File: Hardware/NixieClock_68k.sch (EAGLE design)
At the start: 70 parts, among them IC1 68008, IC10 7805, IC11 MIC803, IC2 AS6C1008, IC3 39SF020, IC4 DS1244Y, IC5 FT245R, IC6 NE555, IC7 ATF1504AS, IC8 74HC374N, IC9 74HC373N, X1 4MHz

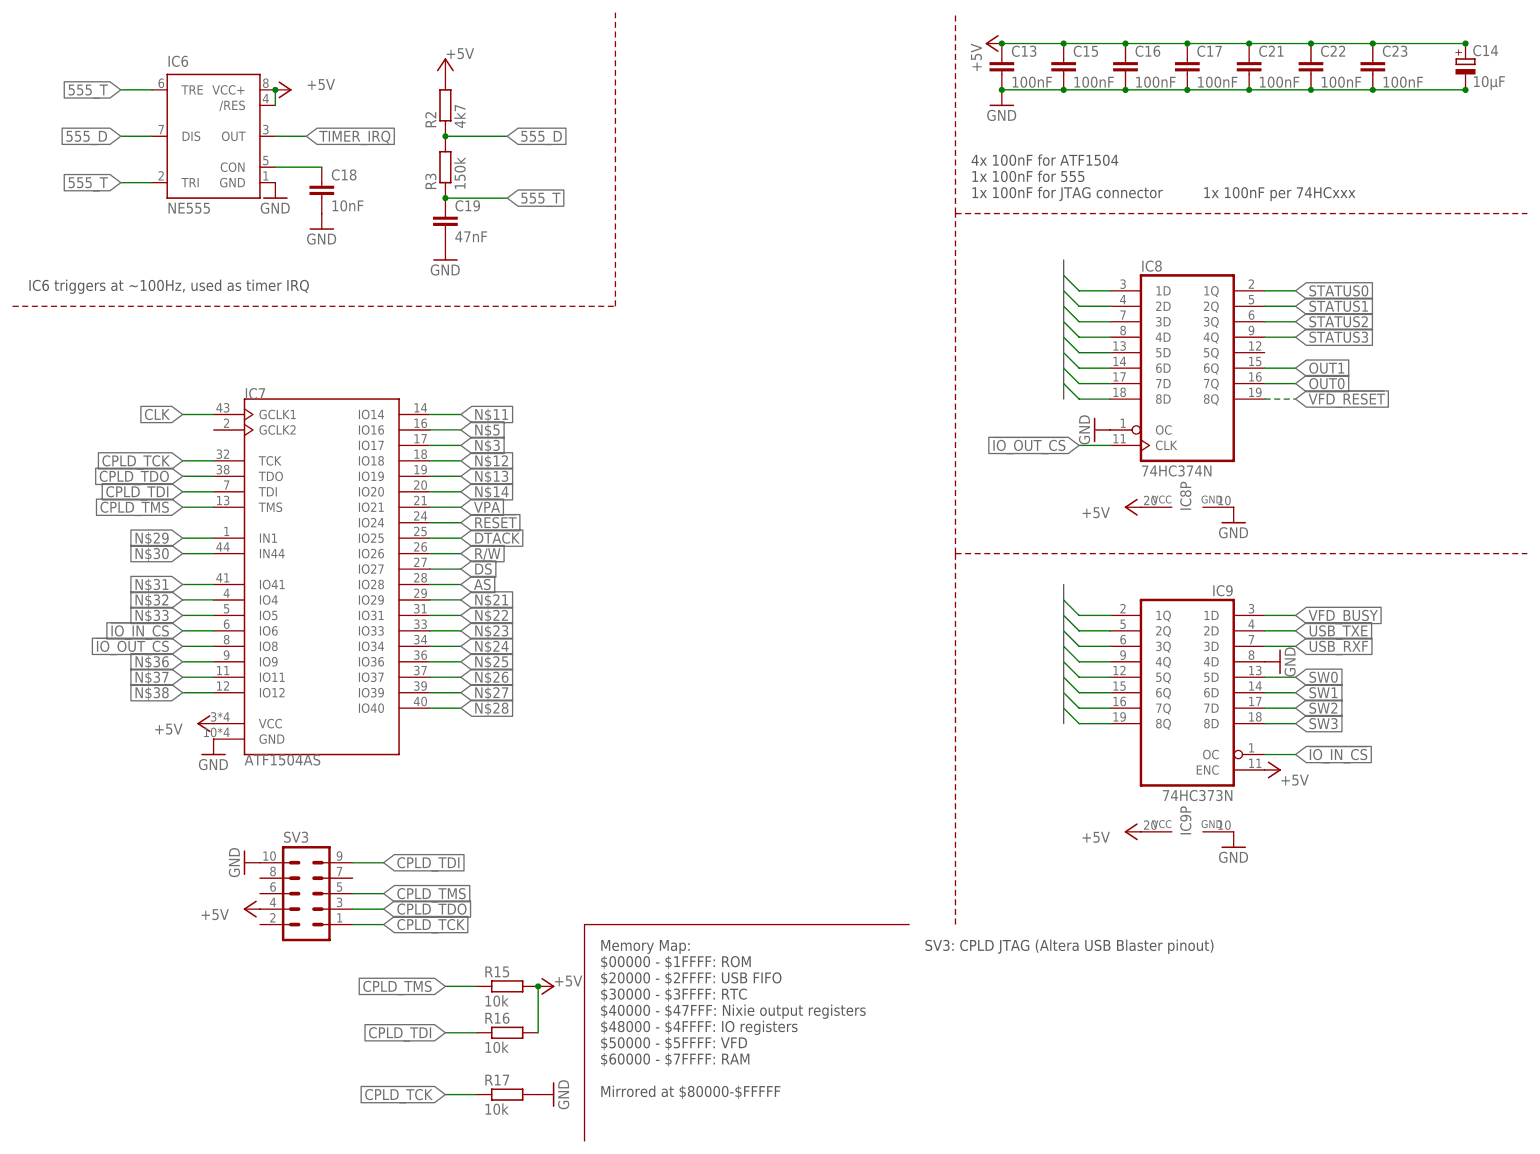
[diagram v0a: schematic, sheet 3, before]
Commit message: replaced cpld with ttl logic
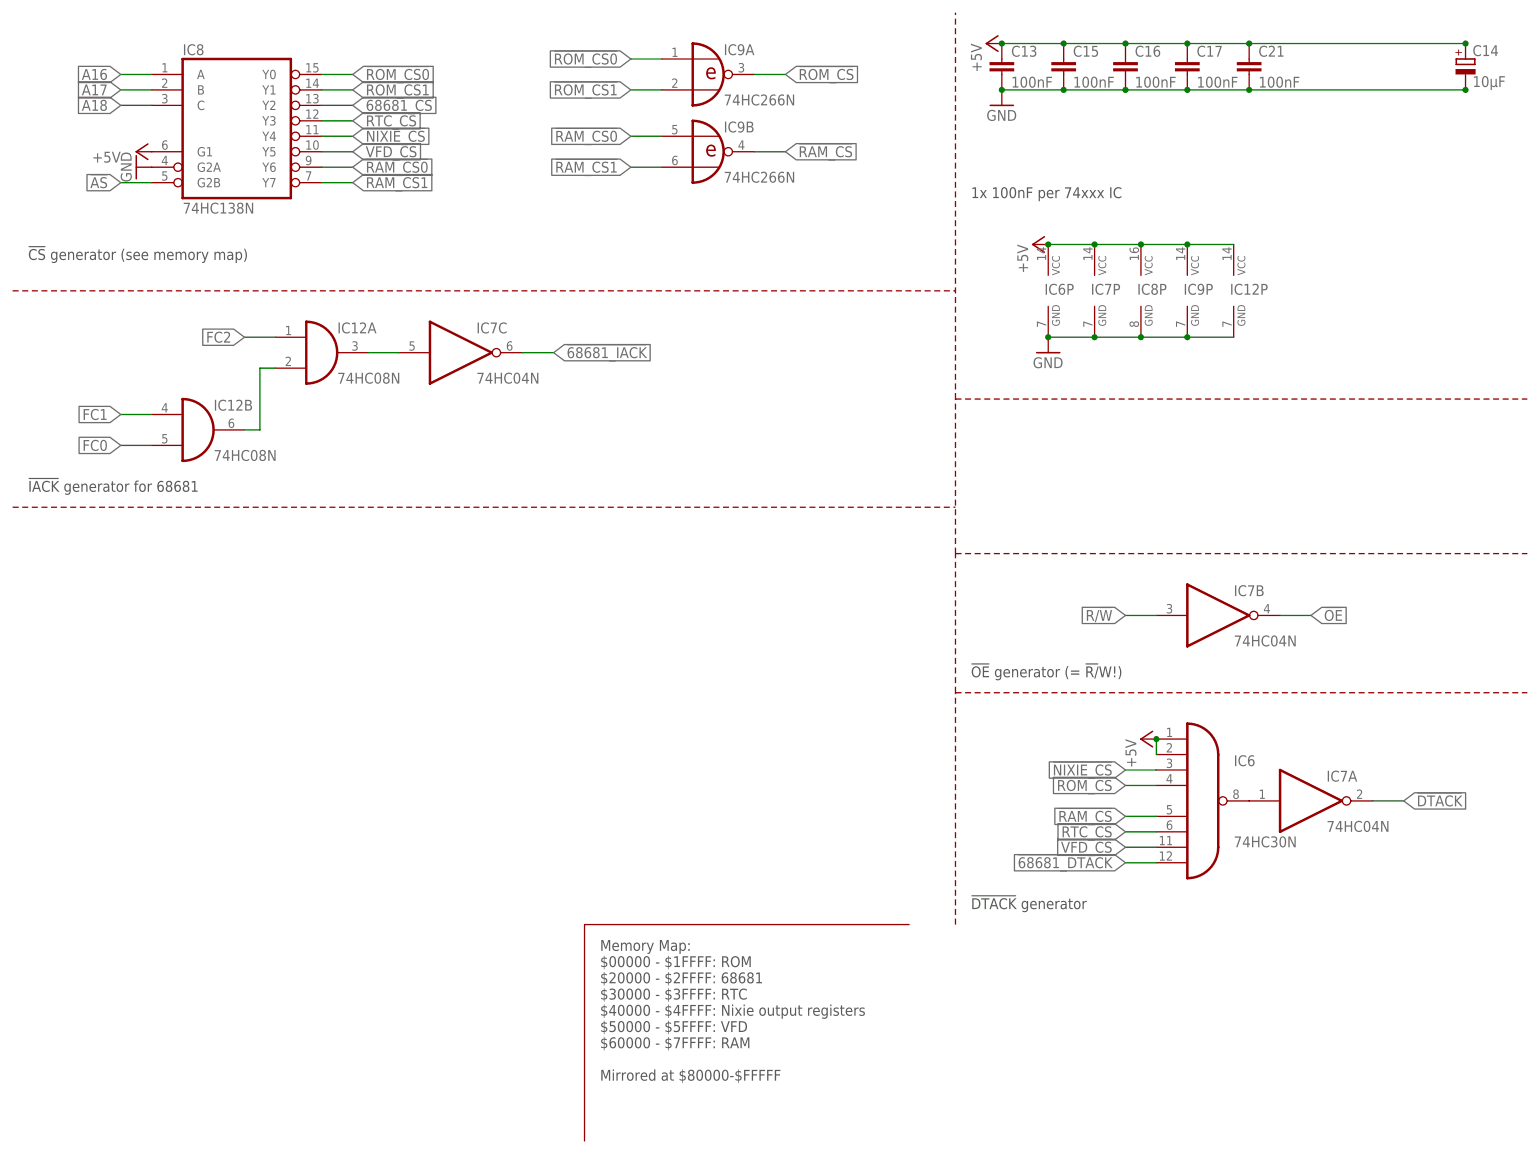
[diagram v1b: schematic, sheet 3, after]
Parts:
- removed C19: 47nF, rcl:C-EUC0805
- removed C22, C23: 100nF, rcl:C-EUC0805
- removed R14, R15, R16, R17, R18, R21, R22, R23, R5, R6: 10k, rcl:R-EU_R2012
- removed R20: 4k7, rcl:R-EU_R2012
- removed R3: 150k, rcl:R-EU_R2012
- removed SV3: (no value), con-lstb:MA05-2
- added IC12: 74HC08N, 74xx-eu:74HC08N
- added Q2: 3.6864MHz, crystal:CRYSTALHC49S
- C12: value 100nF -> 27pF; MOUSER 710-885012207072 -> 77-VJ0805A270GXQCBC
- C18: value 10nF -> 27pF; MOUSER 710-885342207010 -> 77-VJ0805A270GXQCBC
- IC5: value FT245R -> 68681; device Parts:FT245RSSOP-28 -> Parts:MC68681PLCC44-SOCKET
- IC6: value NE555 -> 74HC30N; device st-microelectronics:NE555 -> 74xx-eu:74HC30N; MOUSER 595-NE555P -> 595-CD74HC30E
- IC7: value ATF1504AS -> 74HC04N; device Parts:ATF1504ASPLCC44-SOCKET -> 74xx-eu:74HC04N; MOUSER (none) -> 595-SN74HC04AN
- IC8: value 74HC374N -> 74HC138N; device 74xx-eu:74HC374N -> 74xx-eu:74HC138N; MOUSER 595-SN74HC574N -> 595-SN74HC138N
- IC9: value 74HC373N -> 74HC266N; device 74xx-eu:74HC373N -> 74xx-eu:74HC266N; MOUSER 595-SN74HC373N -> 595-SN74HC266N
- R1: value 10k -> 100R; MOUSER 652-CR0805FX-1002ELF -> 652-CR0805FX-1000ELF
- R2: value 4k7 -> 100R; MOUSER 652-CR0805-JW-472ELF -> 652-CR0805FX-1000ELF
- SV5: value PN61729-S -> (none); device con-berg:PN61729-S -> con-lstb:MA04-2; MOUSER 649-61729-0010BLF -> (none)
- renumbered X1 to Q1
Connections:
- removed net !BERR: IC1.BERR, R14.1
- removed net !BR: IC1.BR, R18.1
- removed net !IO_IN_CS: IC7.IO6, IC9A.OC
- removed net !IO_OUT_CS: IC7.IO8, IC8A.CLK
- removed net !USB_PWREN: IC5.!PWREN, R1.1
- removed net !USB_RD: IC5.!RD
- removed net !USB_RESET: IC5.!RESET, R20.1, R21.2
- removed net !USB_RXF: IC5.!RXF, IC9A.3D, R6.1
- removed net !USB_TXE: IC5.!TXE, IC9A.2D, R5.1
- removed net !VFD_WR: SV2.5
- removed net !VPA: IC1.VPA, IC7.IO21, R22.1
- removed net 555_D: IC6.DIS, R2.1, R3.2
- removed net 555_T: C19.1, IC6.TRE, IC6.TRI, R3.1
- removed net CPLD_TCK: IC7.TCK, R17.1, SV3.1
- removed net CPLD_TDI: IC7.TDI, R16.1, SV3.9
- removed net CPLD_TDO: IC7.TDO, SV3.3
- removed net CPLD_TMS: IC7.TMS, R15.1, SV3.5
- removed net N$10: R20.2, SV5.1
- removed net N$12: IC7.IO18
- removed net N$13: IC7.IO19
- removed net N$14: IC7.IO20
- removed net N$21: IC7.IO29
- removed net N$22: IC7.IO31
- removed net N$23: IC7.IO33
- removed net N$24: IC7.IO34
- removed net N$25: IC7.IO36
- removed net N$26: IC7.IO37
- removed net N$27: IC7.IO39
- removed net N$28: IC7.IO40
- removed net N$29: IC7.IN1
- removed net N$30: IC7.IN44
- removed net N$31: IC7.IO41
- removed net N$32: IC7.IO4
- removed net N$33: IC7.IO5
- removed net N$36: IC7.IO9
- removed net N$37: IC7.IO11
- removed net N$38: IC7.IO12
- removed net TIMER_IRQ: IC6.OUT
- removed net USB+: IC5.USBD+, SV5.3
- removed net USB-: IC5.USBD-, SV5.2
- removed net USB_WR: IC5.WR
- new net !68681_CS: IC5.!CS, IC8A.Y2
- new net !68681_DTACK: IC5.!DTACK, IC6A.I7
- new net !68681_IACK: IC5.!IACK, IC7C.O
- new net !RAM_CS0: IC8A.Y6, IC9B.I0
- new net !RAM_CS1: IC8A.Y7, IC9B.I1
- new net !ROM_CS0: IC8A.Y0, IC9A.I0
- new net !ROM_CS1: IC8A.Y1, IC9A.I1
- new net !VFD_CS: IC6A.I6, IC8A.Y5, SV2.5
- new net 68681_X1: IC5.X1/CLK, R2.1
- new net 68681_X2: IC5.X2, R1.2
- new net UART0_RX: IC5.RXDA, SV5.2
- new net UART0_TX: IC5.TXDA, SV5.1
- new net UART1_RX: IC5.RXDB, SV5.4
- new net UART1_TX: IC5.TXDB, SV5.3
- net !AS: now also IC8A.G2B; no longer IC7.IO28
- net !DS: no longer IC7.IO27
- net !DTACK: now also IC7A.O; no longer IC7.IO25, R23.1
- net !IPL1: now also IC5.!INTR
- net !NIXIE_CS: now also IC6A.I2, IC8A.Y4
- net !OE: now also IC7B.O
- net !RAM_CS: now also IC6A.I4, IC9B.O
- net !RESET: now also IC5.!RESET; no longer IC7.IO24
- net !ROM_CS: now also IC6A.I3, IC9A.O
- net !RTC_CS: now also IC6A.I5, IC8A.Y3
- net !VFD_RESET: now also IC5.OP4; no longer IC8A.8Q
- net +5V: now also IC1.BERR, IC1.BR, IC1.VPA, IC12P.VCC, IC6A.I0, IC6A.I1, IC6P.VCC, IC7P.VCC, IC8A.G1, SV5.6, SV5.8; no longer C22.1, C23.1, IC5.VCCIO, IC6./RES, IC6.VCC+, IC7.VCC, IC9A.ENC, R1.2, R14.2, R15.2, R16.2, R18.2, R2.2, R22.2, R23.2, R6.2, SV3.4
- net A0: now also IC5.A1
- net A1: now also IC5.A2
- net A16: now also IC8A.A
- net A17: now also IC8A.B
- net A18: now also IC8A.C
- net A2: now also IC5.A3
- net A3: now also IC5.A4
- net CLK: no longer IC7.GCLK1
- net D0: no longer IC8A.1D, IC9A.1Q
- net D1: no longer IC8A.2D, IC9A.2Q
- net D2: no longer IC8A.3D, IC9A.3Q
- net D3: no longer IC8A.4D, IC9A.4Q
- net D4: no longer IC8A.5D, IC9A.5Q
- net D5: no longer IC8A.6D, IC9A.6Q
- net D6: no longer IC8A.7D, IC9A.7Q
- net D7: no longer IC8A.8D, IC9A.8Q
- net FC0: now also IC12B.I1
- net FC1: now also IC12B.I0
- net FC2: now also IC12A.I0
- net GND: now also C12.2, IC12P.GND, IC6P.GND, IC7P.GND, IC8A.G2A, SV5.5, SV5.7; no longer C12.1, C19.2, C22.2, C23.2, IC5.AGND, IC5.TEST, IC6.GND, IC7.GND, IC8A.OC, IC9A.4D, R17.2, R21.1, R5.2, SV3.10, SV5.4, SV5.S1, SV5.S2
- net N$1: now also C12.1, Q2.2, R1.1; no longer C12.2, IC5.3V3OUT
- net N$11: now also IC12A.I1, IC12B.O; no longer IC7.IO14
- net N$2: now also Q2.1, R2.2; no longer IC6.CON
- net N$3: now also IC6A.O, IC7A.I; no longer IC7.IO17
- net N$5: now also IC12A.O, IC7C.I; no longer IC7.IO16
- net OUT0: no longer IC8A.7Q
- net OUT1: no longer IC8A.6Q
- net R/!W!: now also IC5.R/!W, IC7B.I; no longer IC7.IO26
- net STATUS0: now also IC5.OP0; no longer IC8A.1Q
- net STATUS1: now also IC5.OP1, R7.1; no longer IC8A.2Q
- net STATUS2: now also IC5.OP2; no longer IC8A.3Q, R7.1
- net STATUS3: now also IC5.OP3; no longer IC8A.4Q
- net SW0: now also IC5.IP0; no longer IC9A.5D
- net SW1: now also IC5.IP1; no longer IC9A.6D
- net SW2: now also IC5.IP2; no longer IC9A.7D
- net SW3: now also IC5.IP4; no longer IC9A.8D
- net VFD_BUSY: now also IC5.IP3; no longer IC9A.1D
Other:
- note added: "!CS! generator (see memory map)"
- note added: "!DTACK! generator"
- note added: "!IACK! generator for 68681"
- note added: "!OE! generator (= !R/!W!)"
- note added: "1x 100nF per 74xxx IC"
- note added: "1x 10µF for VFD/Nixie connector 1x 10µF for 68681/DS1244Y 1x 100nF for each IC and connector"
- note added: "Memory Map: $00000 - $1FFFF: ROM $20000 - $2FFFF: 68681 $30000 - $3FFFF: RTC $40000 - $4FFFF: Nixie output registers $50000 - $5FFFF: VFD $60000 - $7FFFF: RAM Mirrored at $80000-$FFFFF"
- note added: "SV5: UARTs"
- note removed: "1x 100nF per 74HCxxx"
- note removed: "1x 10µF for VFD/Nixie connector 1x 10µF for FT245R/DS1244Y 1x 100nF for each IC and connector"
- note removed: "4x 100nF for ATF1504 1x 100nF for 555 1x 100nF for JTAG connector"
- note removed: "IC6 triggers at ~100Hz, used as timer IRQ"
- note removed: "Memory Map: $00000 - $1FFFF: ROM $20000 - $2FFFF: USB FIFO $30000 - $3FFFF: RTC $40000 - $47FFF: Nixie output registers $48000 - $4FFFF: IO registers $50000 - $5FFFF: VFD $60000 - $7FFFF: RAM Mirrored at $80000-$FFFFF"
- note removed: "SV3: CPLD JTAG (Altera USB Blaster pinout)"
- moved on the sheet: C12, IC8P, IC9P, R1
